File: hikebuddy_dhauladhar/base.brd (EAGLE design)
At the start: 75 x 41 mm, 114 parts, among them J1 MF-CON-MICROUSB-RIGHT, J2 GPS Port, J5 SOLDER_PAD_2, U1 LTC3586EUFE-1#PBF, U2 MAX17260SETD+, U3 MF-DSC-SOT233-MMBT3904, U4 MF-DSC-SOT233-MMBT3904, U5 DRV2605LTDGSRQ1, U6 BMX160

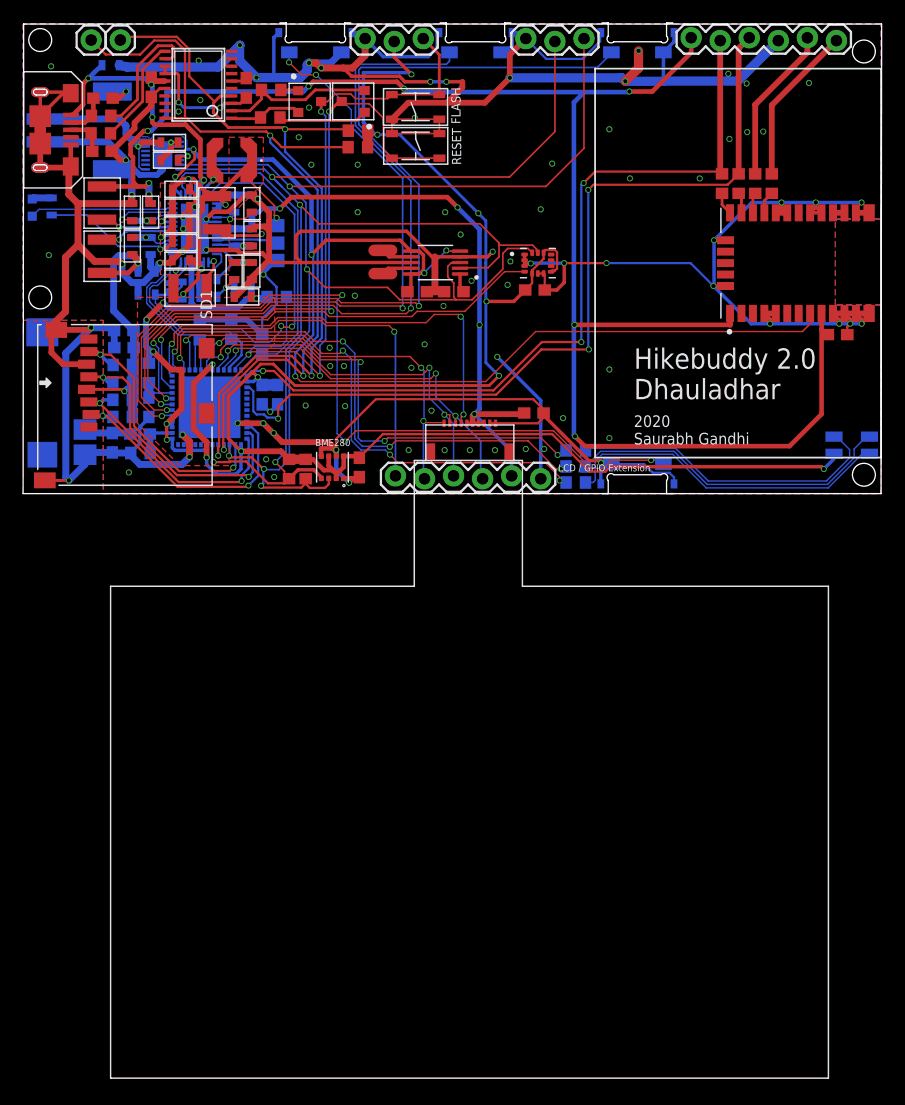
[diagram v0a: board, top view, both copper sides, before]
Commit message: changed sd card to Molex, added pcbway acknowledgement
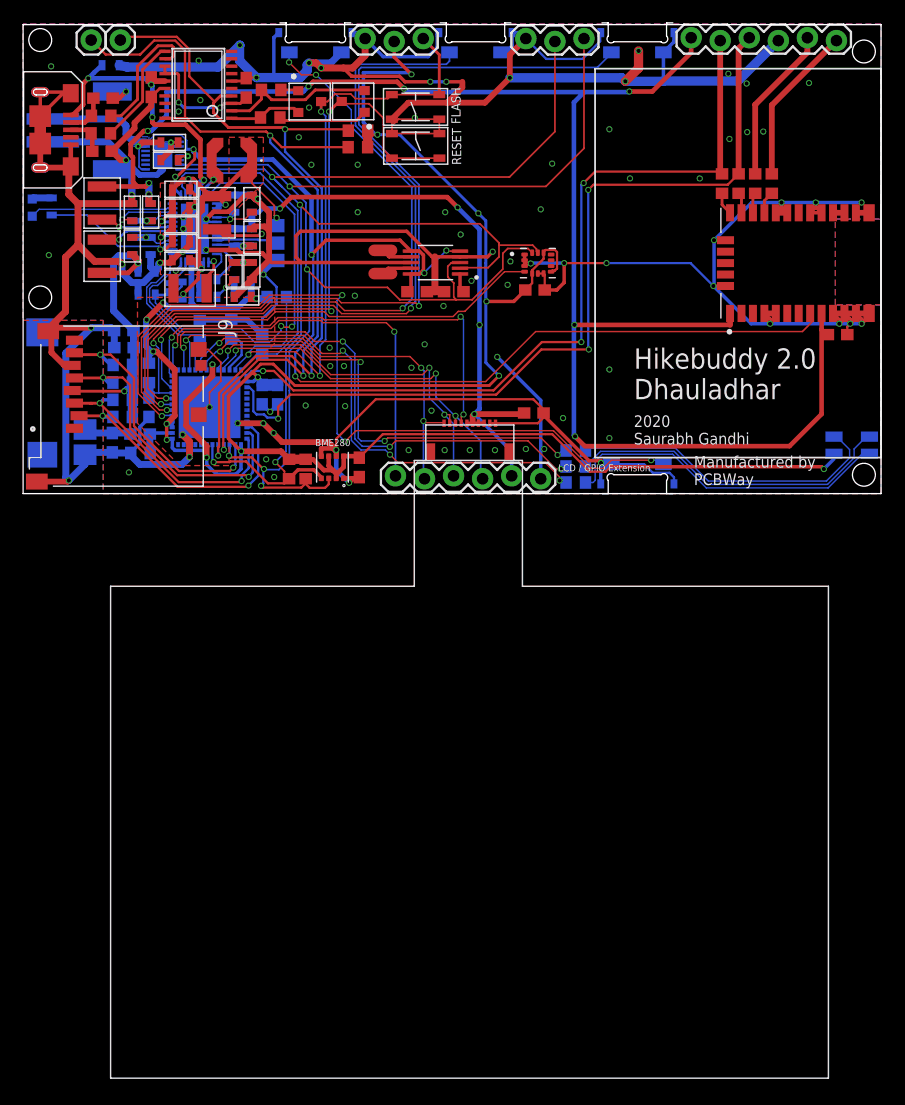
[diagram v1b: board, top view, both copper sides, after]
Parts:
- removed SD1: MF-MICROSD, MF_Connectors:MF-MICROSD
- added J9: 47352-1001, 47352-1001:MOLEX_47352-1001
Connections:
- net 3V3_SDC: now also J9.4; no longer SD1.PIN4
- net GND: now also J9.6, J9.S1, J9.S2, J9.S3, J9.S4; no longer SD1.G0, SD1.G1, SD1.PIN6
- net SD_CLK: now also J9.5; no longer SD1.PIN5
- net SD_CS: now also J9.2; no longer SD1.PIN2
- net SD_MISO: now also J9.7; no longer SD1.PIN7
- net SD_MOSI: now also J9.3; no longer SD1.PIN3
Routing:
- net GND: track 521.2 -> 529.4 mm, vias 97 -> 98
- net SD_CLK: track 25.2 -> 26.4 mm
- net SD_MISO: track 23.1 -> 24.3 mm
- net SD_MOSI: track 21.6 -> 22.8 mm
- net 3V3_SDC: track 27.4 -> 28.6 mm
- net SD_CS: track 23.5 -> 24.5 mm
- net SW3: track 58.6 -> 59.6 mm
- net SW4: track 63.3 -> 64.1 mm
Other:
- outline, holes or cut-outs redrawn
- board text added: "Manufactured by PCBWay"

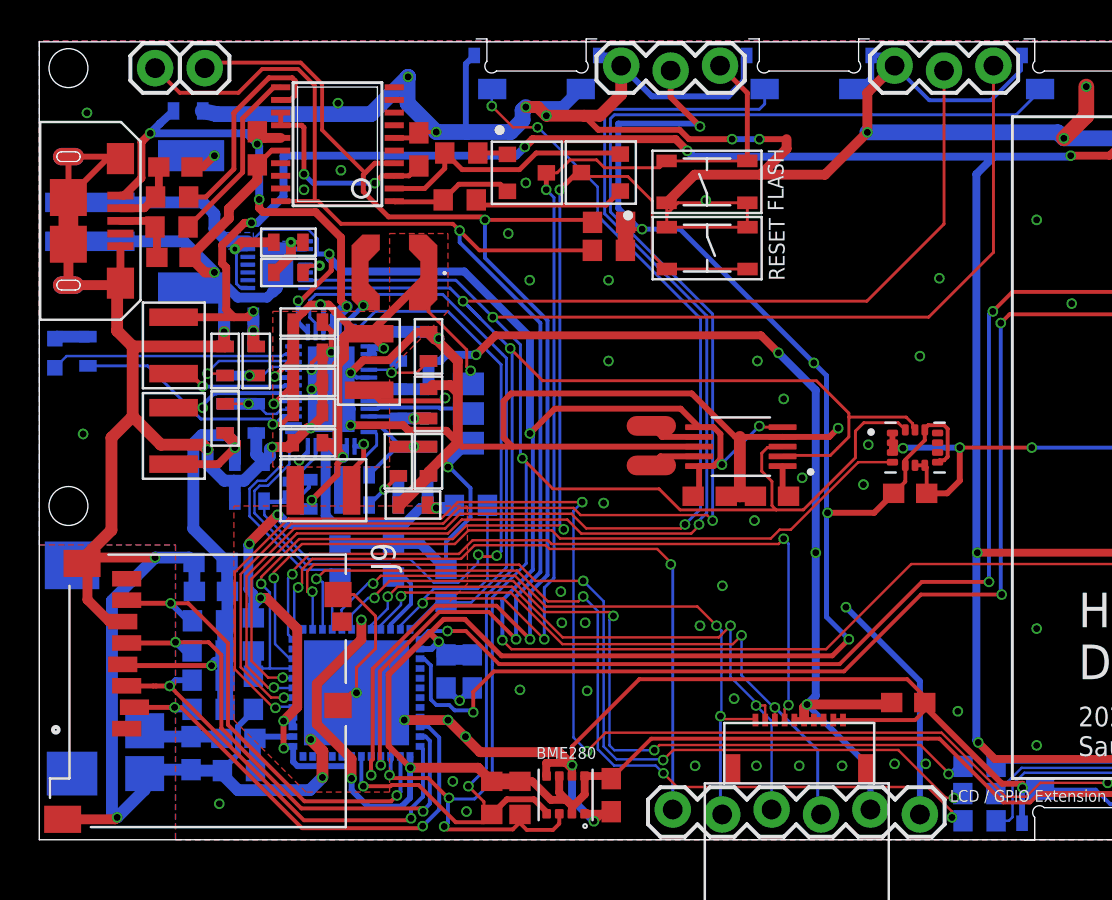
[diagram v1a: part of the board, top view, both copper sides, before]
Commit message: added pullups to buttons, moved jst2 to make room for connector, removed test pads and joined EN to Vreg
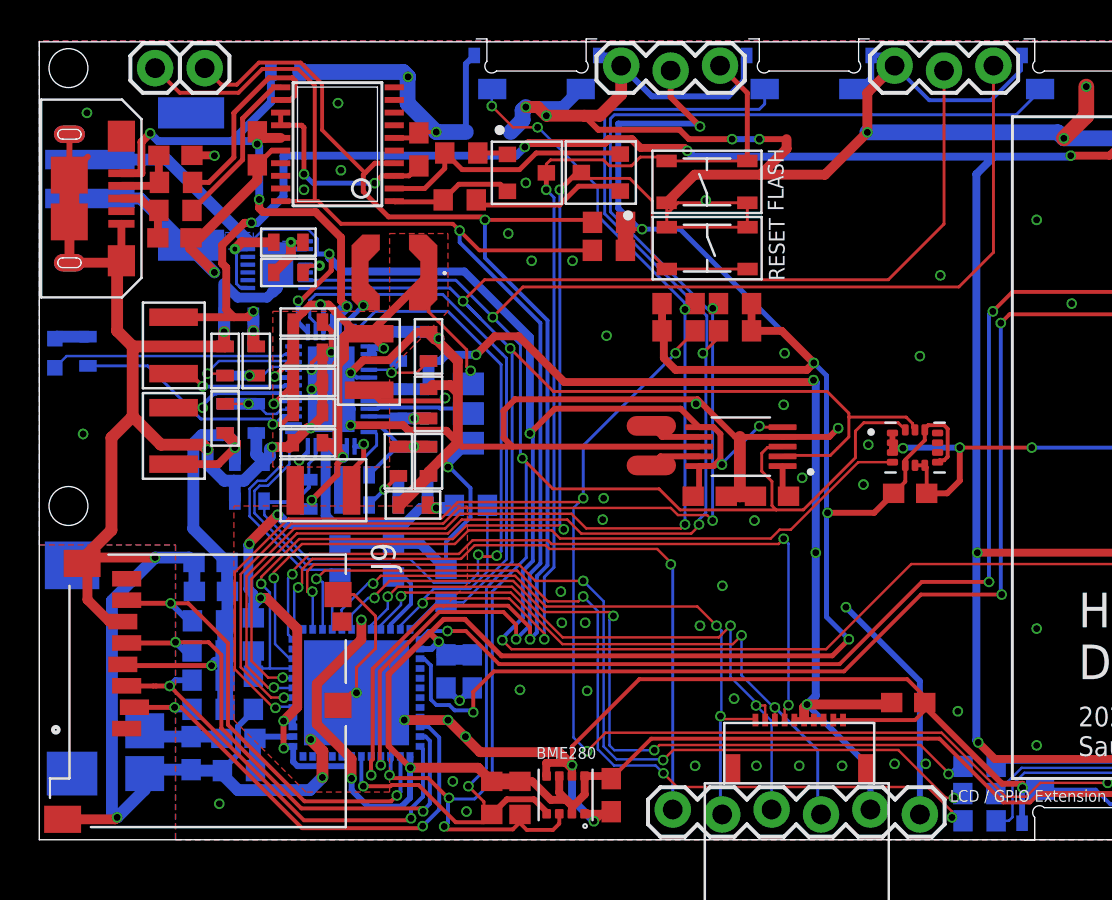
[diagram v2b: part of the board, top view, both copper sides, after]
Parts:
- removed TP1, TP2: TEST-POINT2, SparkFun-Connectors:PAD.02X.02
- added R32, R33, R34, R35: 10k, SparkFun-Resistors:R0603
- moved C9 5.39 mm to (12.7, 39.5)
- moved BATTERY1 2.20 mm to (6.30, 34.0)
- moved J1 1.15 mm to (2.95, 33.0)
- moved C6 1.00 mm to (6.95, 30.9)
- moved R4 0.87 mm to (7.00, 32.3)
- moved R3 0.78 mm to (7.03, 33.8)
- moved C5 0.60 mm to (7.00, 35.2)
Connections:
- removed net N$24: C20.P$2, R16.P$2, TP1.P$1, U1.38
- net N$19: now also C20.P$2, R16.P$2, U1.38; no longer TP2.P$1
- net SW1: now also R32.1
- net SW2: now also R33.1
- net SW3: now also R34.1
- net SW4: now also R35.1
- net VCC: now also R32.2, R33.2, R34.2, R35.2
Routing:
- net N$24: track 38.4 -> 0.00 mm, vias 2 -> 0
- net N$19: track 2.54 -> 39.2 mm, vias 0 -> 2
- net VCC: track 210.0 -> 226.3 mm
- net SW1: track 71.5 -> 82.8 mm, vias 4 -> 5
- net GND: track 529.4 -> 518.5 mm, vias 98 -> 100
- net V_USB: track 27.1 -> 29.1 mm
- net SW4: track 64.1 -> 65.7 mm, vias 2 -> 3
- net ESP_TX: track 67.1 -> 68.2 mm
- net N$7: track 9.36 -> 8.43 mm
- net N$6: track 11.4 -> 10.5 mm
- net SW2: track 79.7 -> 80.4 mm, vias 2 -> 3
- net SW3: vias 4 -> 5

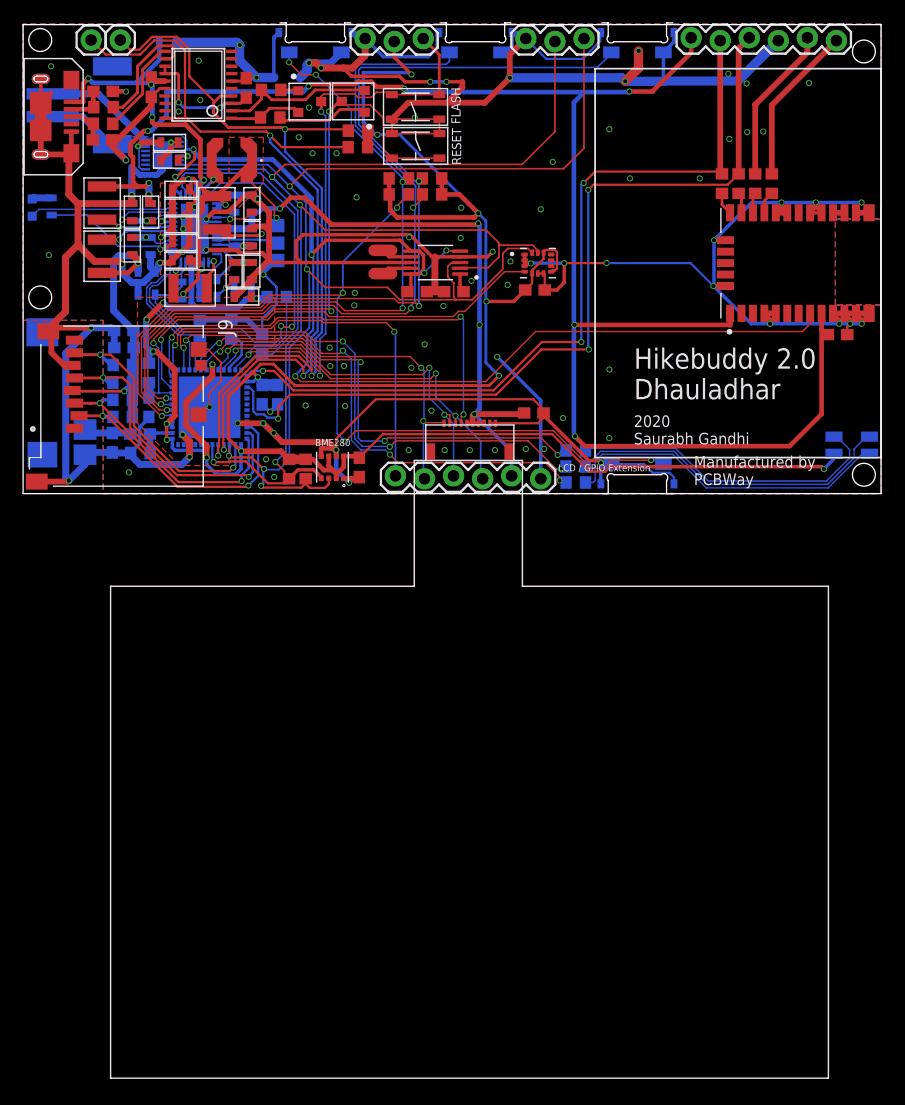
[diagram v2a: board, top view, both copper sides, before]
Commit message: moved LCD and jst2 a little bit to fit everything
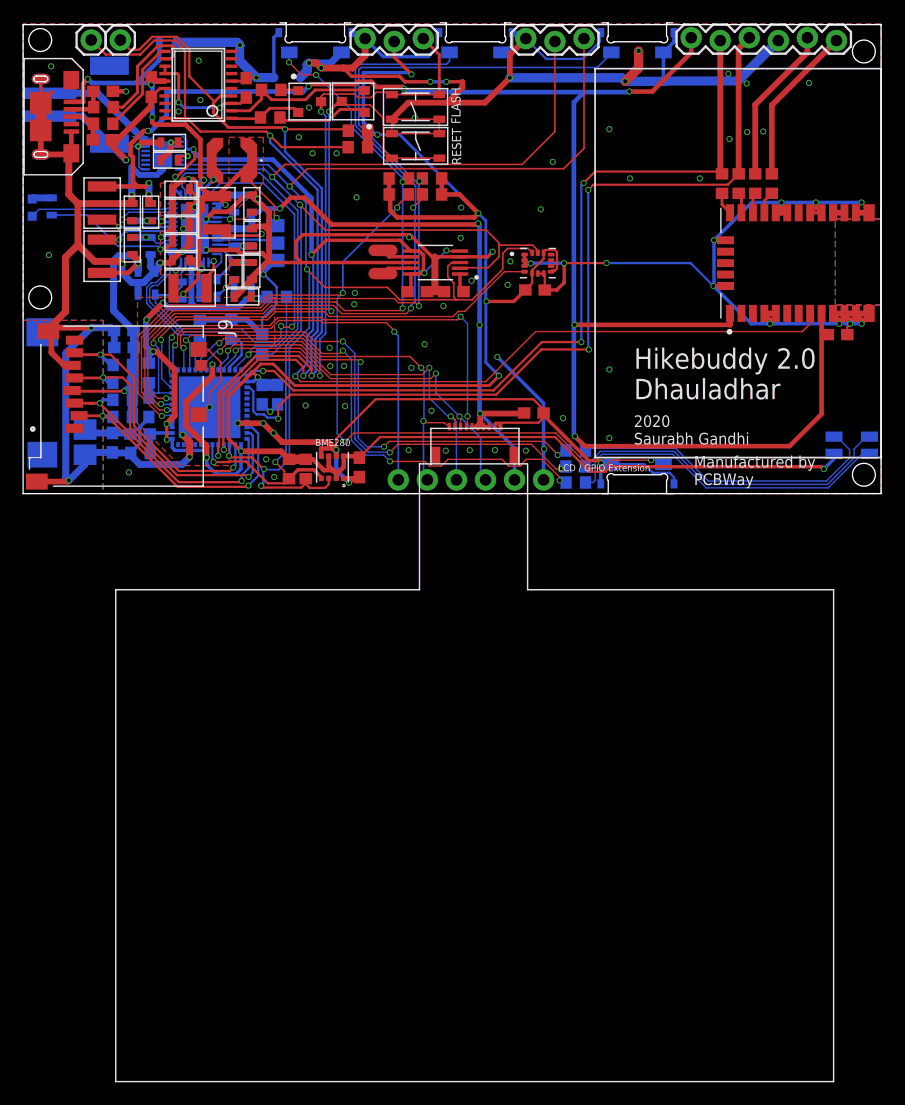
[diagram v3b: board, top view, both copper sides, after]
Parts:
- J8: device SparkFun-Connectors:1X06_LOCK -> SparkFun-Connectors:1X06_NO_SILK
- moved U$5 0.54 mm to (39.5, 0.60)
- moved J8 0.27 mm to (45.5, 1.20)
- moved BATTERY1 0.25 mm to (6.05, 34.0)
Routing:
- net LED2: track 46.2 -> 47.2 mm
- net LCD_CLK: track 33.8 -> 34.6 mm
- net GND: track 518.5 -> 519.1 mm
